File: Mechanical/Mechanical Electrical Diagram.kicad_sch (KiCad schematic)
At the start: 21 parts

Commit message: Updated Mechanical Diagram
Blah Blah Blah
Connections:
- net at U11.1 (M+_(Red)), U19.1 (M+_(Red)), U6.1 (M+_(Red))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: now also U18.2 (M-)
- net at U16.2 (M-): now also U10.1 (M+_(Red)), U17.1 (M+_(Red)), U4.1 (M+_(Red)), U5.1 (M+_(Red))
- net at U14.2 (M-): now also U15.1 (M+_(Red)), U2.1 (M+_(Red)), U3.1 (M+_(Red)), U9.1 (M+_(Red))
- net at U12.1 (M+_(Red)), U21.1 (M+_(Red)), U8.1 (M+_(Red)): now also U20.2 (M-)
- net at U13.2 (M-): now also U1.1 (M+_(Red))
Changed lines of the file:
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@@
-	)
-	(junction
-		(at 143.51 347.98)
-		(diameter 0)
-		(color 0 0 0 0)
 	)
 	(junction
@@
 	)
 	(junction
-		(at 209.55 347.98)
-		(diameter 0)
-		(color 0 0 0 0)
-	)
-	(junction
-		(at 151.13 347.98)
-		(diameter 0)
-		(color 0 0 0 0)
-	)
-	(junction
 		(at 318.77 351.79)
 		(diameter 0)
@@
 	)
 	(junction
-		(at 151.13 351.79)
-		(diameter 0)
-		(color 0 0 0 0)
-	)
-	(junction
 		(at 260.35 351.79)
 		(diameter 0)
@@
 	)
 	(junction
-		(at 201.93 351.79)
-		(diameter 0)
-		(color 0 0 0 0)
-	)
-	(junction
 		(at 304.8 331.47)
 		(diameter 0)
@@
 	(wire
 		(pts
+			(xy 140.97 288.29) (xy 140.97 304.8)
+		)
+		(stroke
+			(width 0)
+			(type default)
+		)
+	)
+	(wire
+		(pts
 			(xy 328.93 266.7) (xy 328.93 275.59)
 		)
@@
 	(wire
 		(pts
-			(xy 82.55 303.53) (xy 82.55 288.29)
+			(xy 82.55 288.29) (xy 82.55 304.8)
 		)
 		(stroke
@@
 	(wire
 		(pts
-			(xy 140.97 303.53) (xy 140.97 288.29)
-		)
-		(stroke
-			(width 0)
-			(type default)
-		)
-	)
-	(wire
-		(pts
 			(xy 264.16 304.8) (xy 264.16 285.75)
 		)
@@
 	(wire
 		(pts
+			(xy 199.39 288.29) (xy 199.39 304.8)
+		)
+		(stroke
+			(width 0)
+			(type default)
+		)
+	)
+	(wire
+		(pts
+			(xy 257.81 288.29) (xy 257.81 304.8)
+		)
+		(stroke
+			(width 0)
+			(type default)
+		)
+	)
+	(wire
+		(pts
 			(xy 95.25 279.4) (xy 95.25 304.8)
 		)
@@
 	(wire
 		(pts
-			(xy 257.81 303.53) (xy 257.81 288.29)
-		)
-		(stroke
-			(width 0)
-			(type default)
-		)
-	)
-	(wire
-		(pts
 			(xy 251.46 288.29) (xy 251.46 267.97)
 		)
@@
 	(wire
 		(pts
-			(xy 316.23 303.53) (xy 316.23 288.29)
+			(xy 316.23 288.29) (xy 316.23 304.8)
 		)
 		(stroke
@@
 		)
 		(stroke
-			(width 0)
-			(type default)
-		)
-	)
-	(wire
-		(pts
-			(xy 199.39 303.53) (xy 199.39 288.29)
-		)
-		(stroke

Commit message: Update Mechanical Electrical Diagram.kicad_sch
Updated Mechanical Electrical Diagram
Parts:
- removed U10, U11, U15, U17, U19, U2, U21, U4, U6, U8: ~, symbol Lunabotics 2025-26:Spark_Max_Motor_Controller
- removed U14, U16, U18, U20: ~, symbol Lunabotics 2025-26:Rev_Neo
- added U10, U11, U15, U2, U4, U6, U8: ~, symbol Lunabotics 2025-26:Rev_Neo
- added U14, U16: ~, symbol Lunabotics 2025-26:Spark_Max_Motor_Controller
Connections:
- net +12V: now also U14.4 (V+), U16.4 (V+)
- net GND: now also U14.5 (V-), U16.5 (V-)
- net at U7.1 (M+_(Red)): now also U9.1 (M+_(Red)), U6.2 (M-), U8.2 (M-)
- net at U7.2 (M-_(Black)): now also U9.2 (M-_(Black)), U6.1 (M+), U8.1 (M+)
- net at U7.3 (Brushless_(White)): now also U9.3 (Brushless_(White)), U6.3 (C), U8.3 (C)
- net at U7.9 (Encoder_Sensor_(6Pin)): now also U9.9 (Encoder_Sensor_(6Pin))
- net at U5.2 (M-_(Black)): now also U3.2 (M-_(Black)), U2.1 (M+), U4.1 (M+)
- net at U5.1 (M+_(Red)): now also U3.1 (M+_(Red)), U2.2 (M-), U4.2 (M-)
- net at U5.3 (Brushless_(White)): now also U3.3 (Brushless_(White)), U2.3 (C), U4.3 (C)
- net at U5.9 (Encoder_Sensor_(6Pin)): now also U3.9 (Encoder_Sensor_(6Pin))
- net at U12.1 (M+_(Red)): now also U10.2 (M-), U11.2 (M-), U14.1 (M+_(Red))
- net at U12.2 (M-_(Black)): now also U10.1 (M+), U11.1 (M+), U14.2 (M-_(Black))
- net at U12.3 (Brushless_(White)): now also U10.3 (C), U11.3 (C), U14.3 (Brushless_(White))
- net at U12.9 (Encoder_Sensor_(6Pin)): now also U14.9 (Encoder_Sensor_(6Pin))
- net at U13.4 (Enc_Cable): no longer U1.9 (Encoder_Sensor_(6Pin))
- new net: U6.4 (Enc_Cable), U8.4 (Enc_Cable)
- new net: U2.4 (Enc_Cable), U4.4 (Enc_Cable)
- new net: U15.2 (M-), U16.1 (M+_(Red))
- new net: U15.1 (M+), U16.2 (M-_(Black))
- new net: U15.3 (C), U16.3 (Brushless_(White))
- new net: U10.4 (Enc_Cable), U11.4 (Enc_Cable)

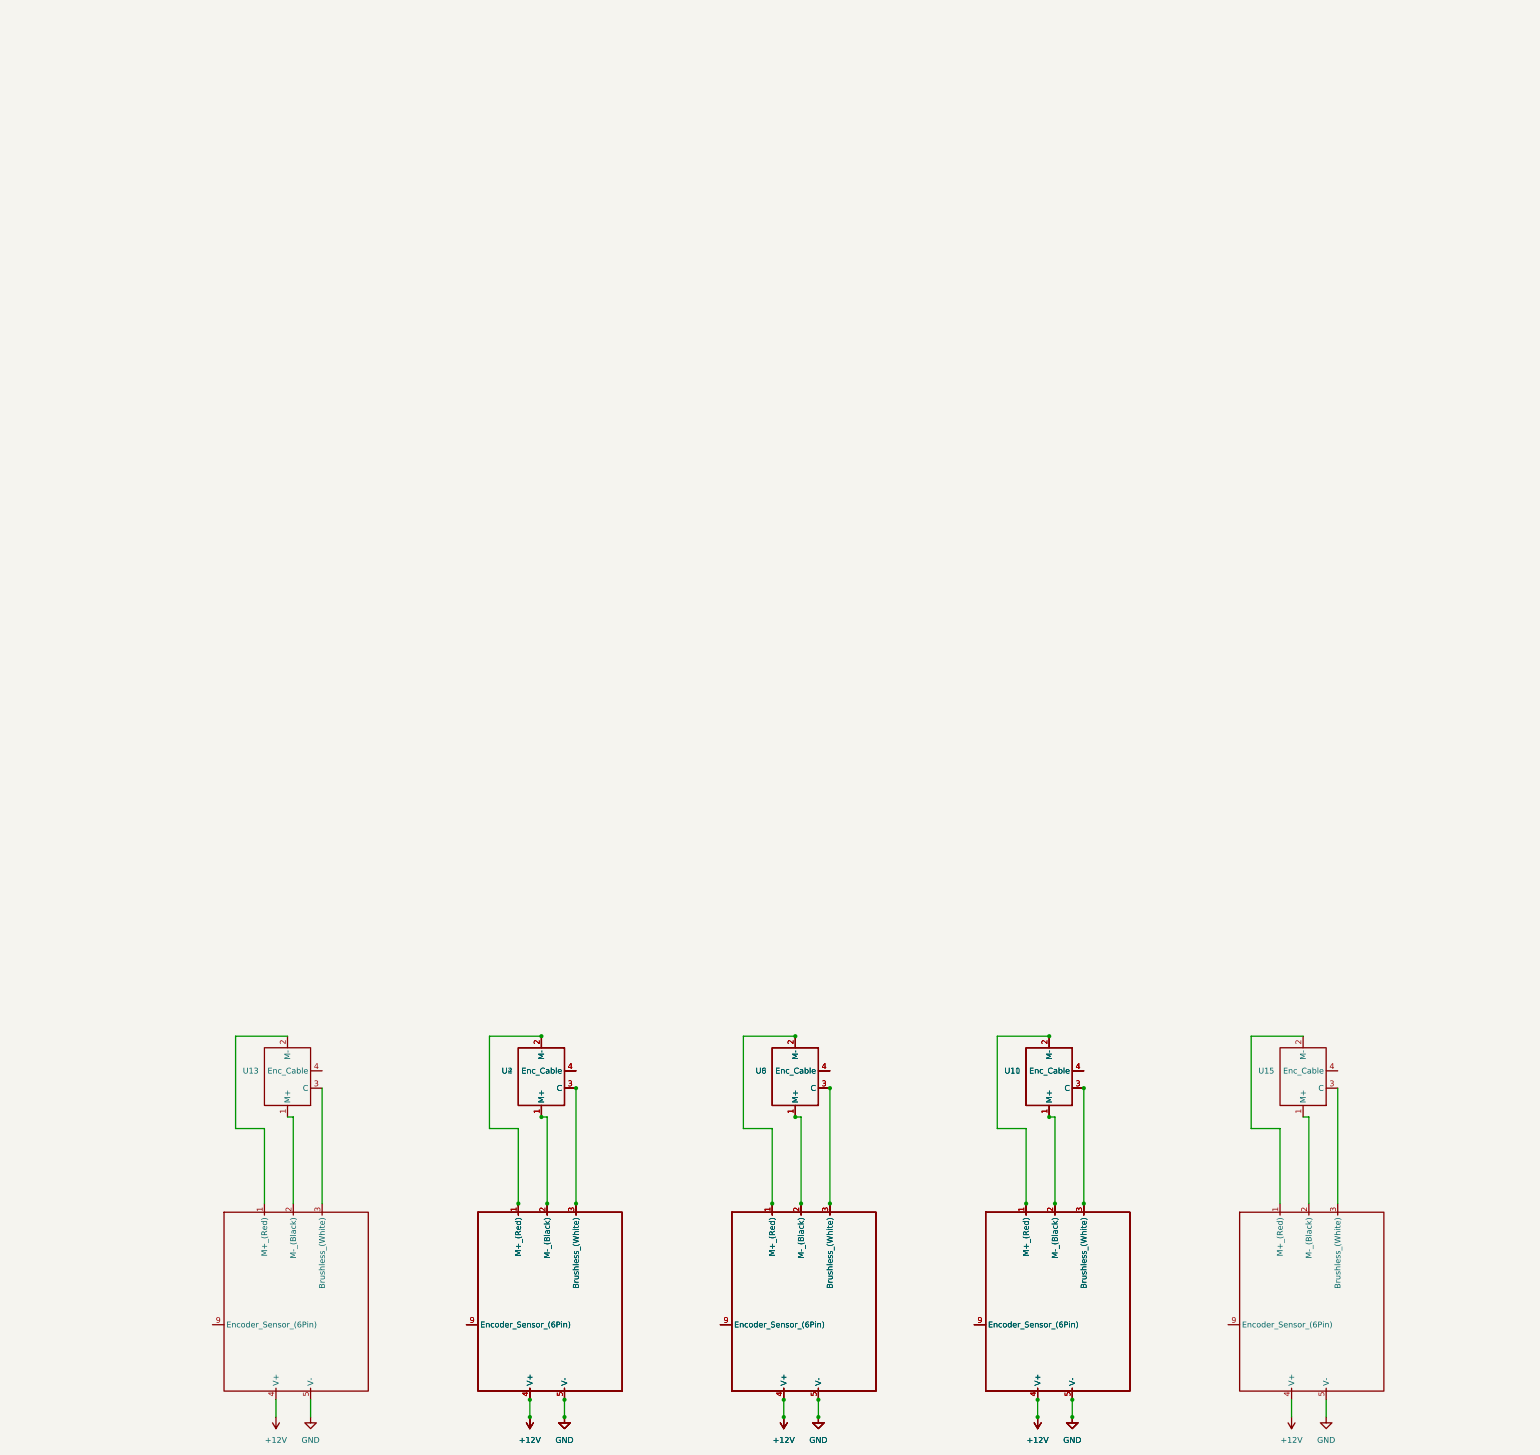
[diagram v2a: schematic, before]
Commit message: Completed Schematics
Only thing not included is a linear actuator and motor controller. Waiting on Mechanical to give us what they want to use
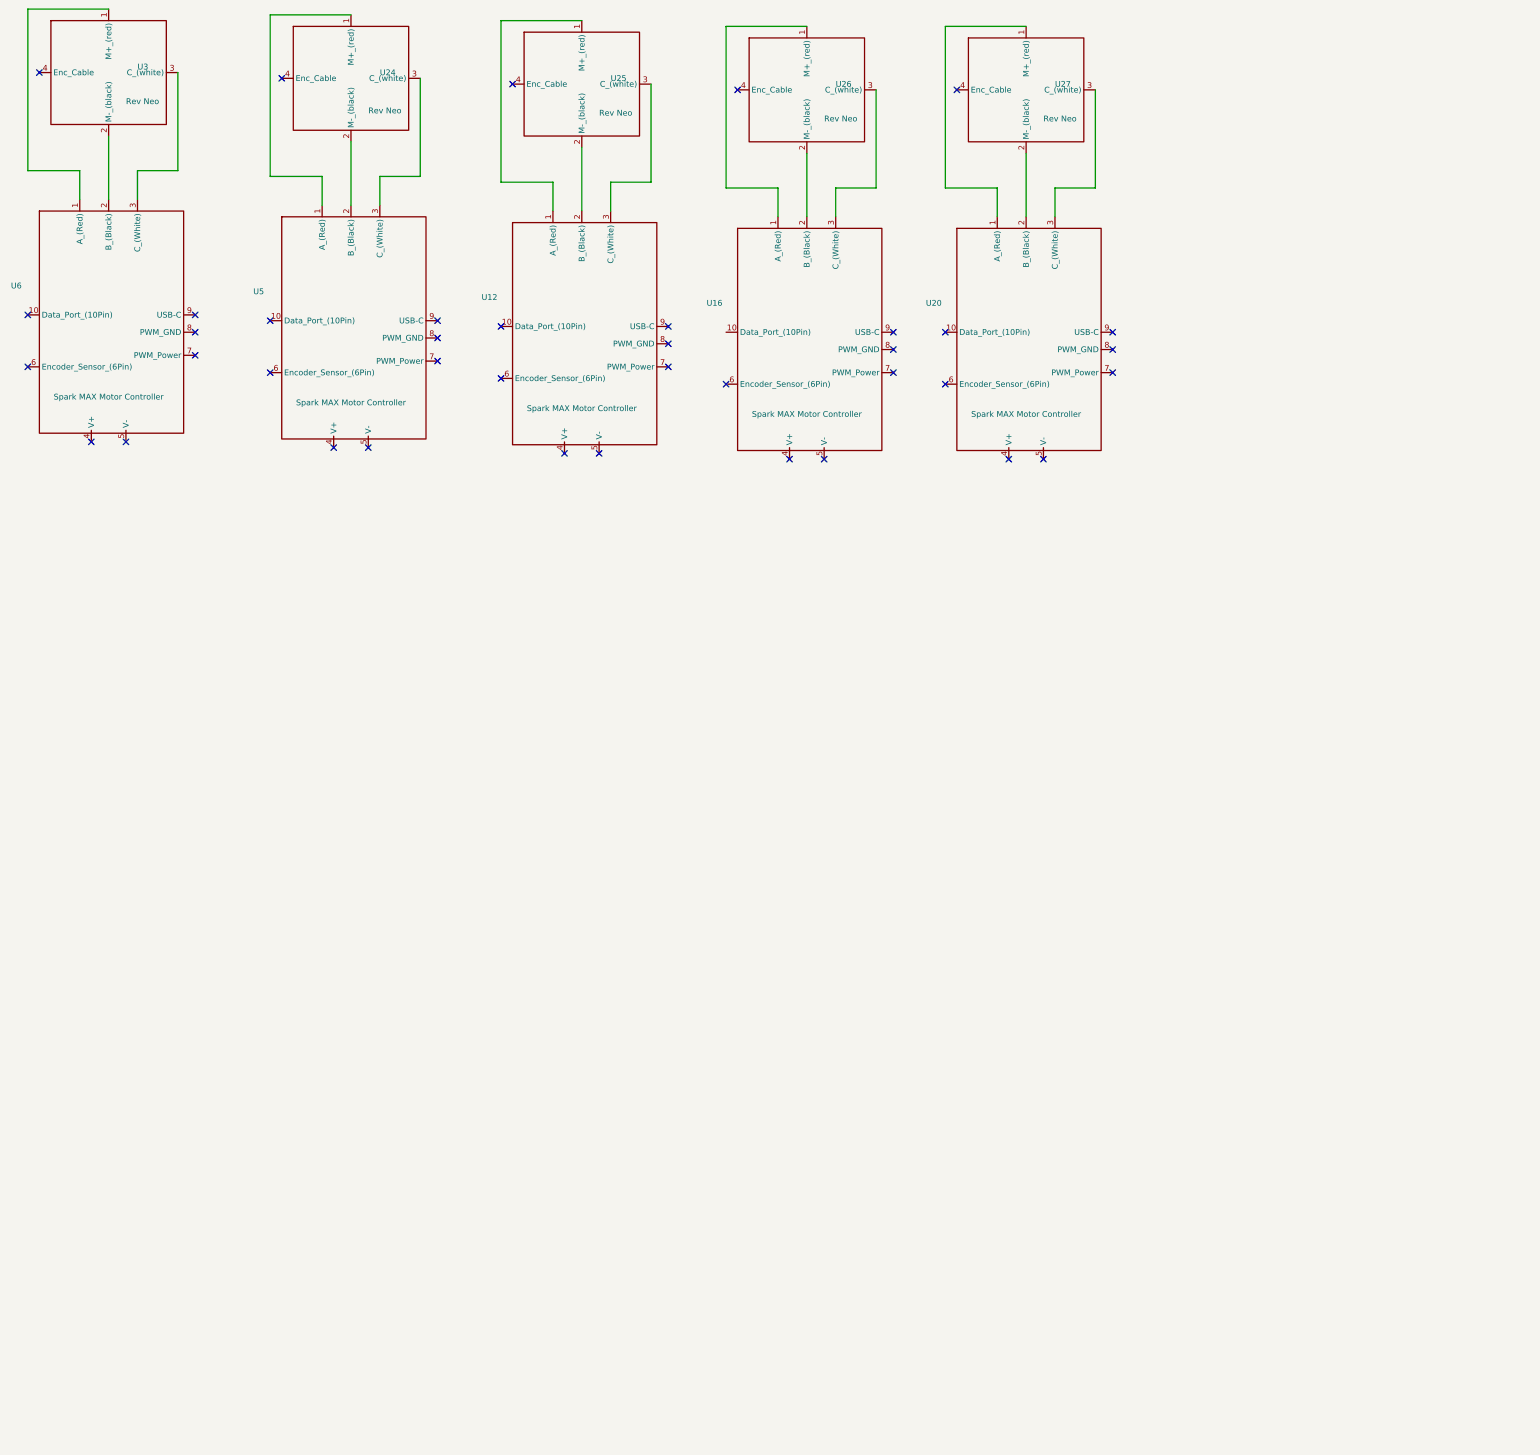
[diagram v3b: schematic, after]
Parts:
- removed U1, U12, U14, U16, U3, U5, U7, U9: ~, symbol Lunabotics 2025-26:Spark_Max_Motor_Controller
- removed U10, U11, U13, U15, U2, U4, U6, U8: ~, symbol Lunabotics 2025-26:Rev_Neo
- added U12, U16, U20, U5, U6: Spark MAX Motor Controller, symbol Lunabotics 2025-26:Spark_MAX_Motor_Controller
- added U24, U25, U26, U27, U3: Rev Neo, symbol Lunabotics 2025-26:Rev_Neo
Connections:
- new net: U20.1 (A_(Red)), U27.1 (M+_(red))
- new net: U20.2 (B_(Black)), U27.2 (M-_(black))
- new net: U20.3 (C_(White)), U27.3 (C_(white))
- new net: U12.1 (A_(Red)), U25.1 (M+_(red))
- new net: U12.2 (B_(Black)), U25.2 (M-_(black))
- new net: U12.3 (C_(White)), U25.3 (C_(white))
- new net: U3.1 (M+_(red)), U6.1 (A_(Red))
- new net: U3.2 (M-_(black)), U6.2 (B_(Black))
- new net: U3.3 (C_(white)), U6.3 (C_(White))
- new net: U16.1 (A_(Red)), U26.1 (M+_(red))
- new net: U16.2 (B_(Black)), U26.2 (M-_(black))
- new net: U16.3 (C_(White)), U26.3 (C_(white))
- new net: U24.1 (M+_(red)), U5.1 (A_(Red))
- new net: U24.2 (M-_(black)), U5.2 (B_(Black))
- new net: U24.3 (C_(white)), U5.3 (C_(White))
- no-connect marks 0 -> 39

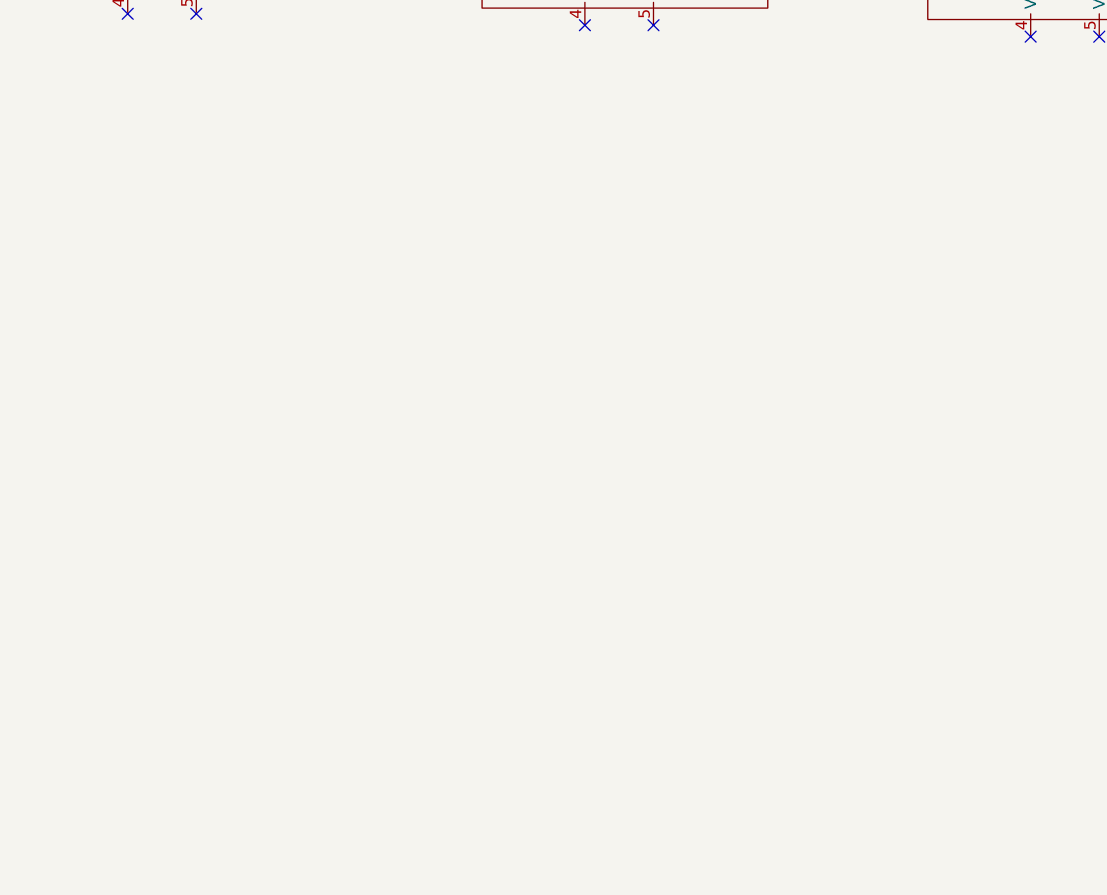
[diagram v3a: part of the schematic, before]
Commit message: Ported Linear Actuator to other schematics
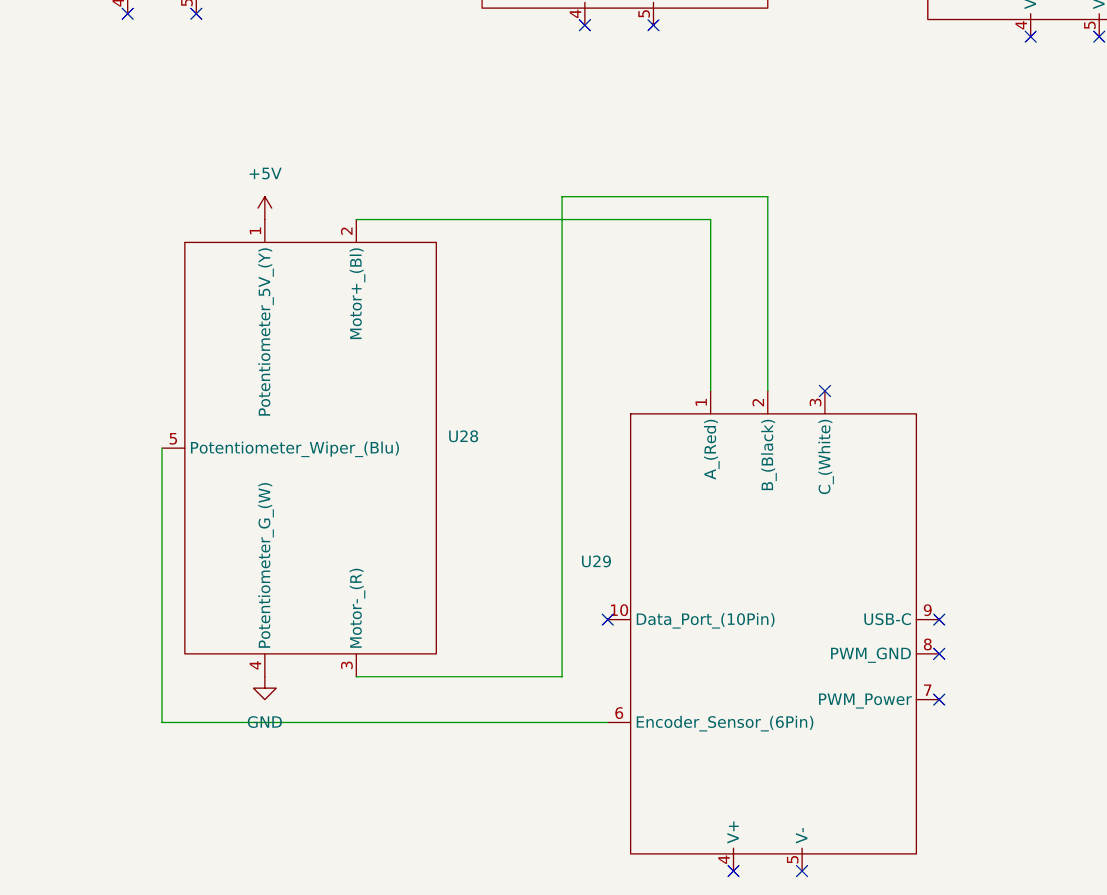
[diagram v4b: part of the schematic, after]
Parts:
- added U28: ~, symbol Lunabotics 2025-26:Feedback_Linear_Actuator
- added U29: ~, symbol Lunabotics 2025-26:Spark_MAX_Motor_Controller
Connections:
- new net: U28.2 (Motor+_(Bl)), U29.1 (A_(Red))
- new net: U28.3 (Motor-_(R)), U29.2 (B_(Black))
- new net: U28.5 (Potentiometer_Wiper_(Blu)), U29.6 (Encoder_Sensor_(6Pin))
- new net +5V: U28.1 (Potentiometer_5V_(Y))
- new net GND: U28.4 (Potentiometer_G_(W))
- no-connect marks 39 -> 46
